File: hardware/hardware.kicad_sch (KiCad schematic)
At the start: 15 parts, among them J1 Screw_Terminal_01x02, J2 Screw_Terminal_01x02, J3 Screw_Terminal_01x02, K1 RM85-2011-35-1005, K2 RM85-2011-35-1005, Q1 BC337, Q2 BC337, U1 XIAO-ESP32-C6

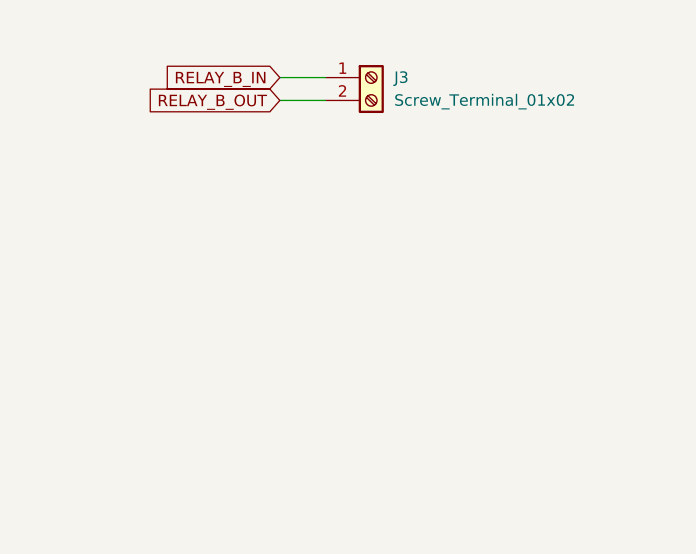
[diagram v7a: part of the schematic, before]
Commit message: Added mounting holes
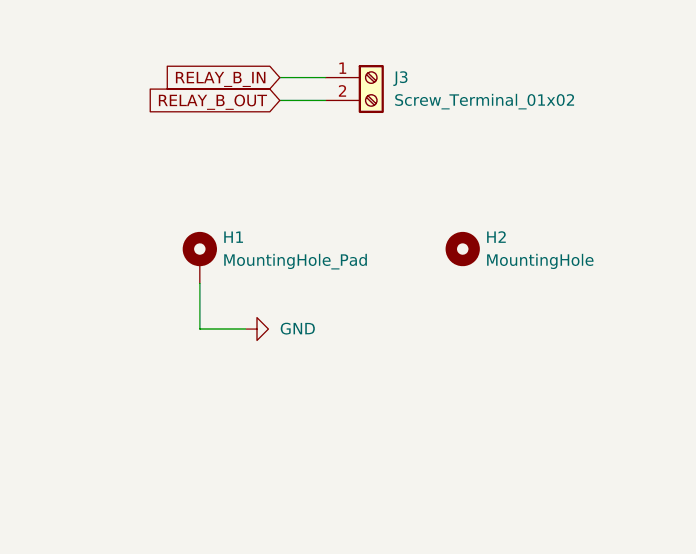
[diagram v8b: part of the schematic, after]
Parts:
- added H1: MountingHole_Pad, MountingHole:MountingHole_2.2mm_M2_Pad, symbol Mechanical:MountingHole_Pad
- added H2: MountingHole, MountingHole:MountingHole_2.2mm_M2, symbol Mechanical:MountingHole
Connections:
- net GND: now also H1.1
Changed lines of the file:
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@@
+	(wire
+		(pts
+			(xy 166.37 109.22) (xy 166.37 114.3)
+		)
+		(stroke
+			(width 0)
+			(type default)
+		)
+	)
 	(wire
 		(pts
@@
 		(pts
 			(xy 35.56 92.71) (xy 39.37 92.71)
+		)
+		(stroke
+			(width 0)
+			(type default)
+		)
+	)
+	(wire
+		(pts
+			(xy 166.37 114.3) (xy 171.45 114.3)
 		)
 		(stroke
@@
 				(justify left)
 				(hide yes)
+			)
+		)
+	)
+	(symbol
+		(lib_id "Mechanical:MountingHole")
+		(at 195.58 105.41 0)
+		(unit 1)
+		(exclude_from_sim no)
+		(in_bom no)
+		(on_board yes)
+		(dnp no)
+		(fields_autoplaced yes)
+		(property "Reference" "H2"
+			(at 198.12 104.1399 0)
+			(effects
+				(font
+					(size 1.27 1.27)
+				)
+				(justify left)
+			)
+		)
+		(property "Value" "MountingHole"
+			(at 198.12 106.6799 0)
+			(effects
+				(font
+					(size 1.27 1.27)
+				)
+				(justify left)
+			)
+		)
+		(property "Footprint" "MountingHole:MountingHole_2.2mm_M2"
+			(at 195.58 105.41 0)
+			(effects
+				(font
+					(size 1.27 1.27)
+				)
+				(hide yes)
+			)
+		)
+		(property "Datasheet" "~"
+			(at 195.58 105.41 0)
+			(effects
+				(font
+					(size 1.27 1.27)
+				)
+				(hide yes)
+			)
+		)
+		(property "Description" "Mounting Hole without connection"
+			(at 195.58 105.41 0)
+			(effects
+				(font
+					(size 1.27 1.27)
+				)
+				(hide yes)
+			)
+		)
+		(instances
+			(project ""
+				(path "/75da26a7-4fdf-42c4-9276-67798e7ef829"
+					(reference "H2")
+					(unit 1)
+				)
 			)
 		)
@@
 	)
 	(symbol
+		(lib_id "power:GND")
+		(at 171.45 114.3 90)
+		(unit 1)
+		(exclude_from_sim no)
+		(in_bom yes)
+		(on_board yes)
+		(dnp no)
+		(fields_autoplaced yes)
+		(property "Reference" "#PWR012"
+			(at 177.8 114.3 0)
+			(effects
+				(font
+					(size 1.27 1.27)
+				)
+				(hide yes)
+			)
+		)
+		(property "Value" "GND"
+			(at 175.26 114.2999 90)
+			(effects
+				(font
+					(size 1.27 1.27)
+				)
+				(justify right)
+			)
+		)
+		(property "Footprint" ""
+			(at 171.45 114.3 0)
+			(effects
+				(font
+					(size 1.27 1.27)
+				)
+				(hide yes)
+			)
+		)
+		(property "Datasheet" ""
+			(at 171.45 114.3 0)
+			(effects
+				(font
+					(size 1.27 1.27)
+				)
+				(hide yes)
+			)
+		)
+		(property "Description" "Power symbol creates a global label with name \"GND\" , ground"
+			(at 171.45 114.3 0)
+			(effects
+				(font
+					(size 1.27 1.27)
+				)
+				(hide yes)
+			)
+		)
+		(pin "1"
+		)
+		(instances
+			(project "hardware"
+				(path "/75da26a7-4fdf-42c4-9276-67798e7ef829"
+					(reference "#PWR012")
+					(unit 1)
+				)
+			)
+		)
+	)
+	(symbol
 		(lib_id "power:+3V3")
 		(at 121.92 31.75 0)
@@
 					(unit 1)
 				)
+			)
+		)
+	)
+	(symbol
+		(lib_id "Mechanical:MountingHole_Pad")
+		(at 166.37 106.68 0)
+		(unit 1)
+		(exclude_from_sim no)
+		(in_bom no)
+		(on_board yes)
+		(dnp no)
+		(fields_autoplaced yes)
+		(property "Reference" "H1"
+			(at 168.91 104.1399 0)
+			(effects
+				(font
+					(size 1.27 1.27)
+				)
+				(justify left)
+			)
+		)
+		(property "Value" "MountingHole_Pad"
+			(at 168.91 106.6799 0)
+			(effects
+				(font
+					(size 1.27 1.27)
+				)
+				(justify left)
+			)
+		)
+		(property "Footprint" "MountingHole:MountingHole_2.2mm_M2_Pad"
+			(at 166.37 106.68 0)
+			(effects
+				(font
+					(size 1.27 1.27)
+				)
+				(hide yes)
+			)
+		)
+		(property "Datasheet" "~"
+			(at 166.37 106.68 0)
+			(effects
+				(font
+					(size 1.27 1.27)
+				)
+				(hide yes)
+			)
+		)
+		(property "Description" "Mounting Hole with connection"
+			(at 166.37 106.68 0)
+			(effects
+				(font
+					(size 1.27 1.27)
+				)
+				(hide yes)
+			)
+		)
+		(pin "1"
+		)
+		(instances
+			(project ""
+				(path "/75da26a7-4fdf-42c4-9276-67798e7ef829"
+					(reference "H1")
+					(unit 1)
+				)
